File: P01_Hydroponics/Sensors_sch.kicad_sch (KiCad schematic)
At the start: 9 parts, among them J2 JST_PH_3P_TEMP, J3 JST_PH_3P_FLOW, J4 JST_PH_3P_WLS1, J5 JST_PH_4P_WLS0, J6 JST_PH_2P_PUMP, Q2 NMOS

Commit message: Need review
Please review the schematics.
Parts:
- removed J4: JST_PH_3P_WLS1, symbol Connector:Conn_01x03_Socket
- removed J5: JST_PH_4P_WLS0, symbol Connector:Conn_01x04_Socket
- added J4: JST_PH_3P_TEMP, symbol Connector:Conn_01x03_Pin
- added J5: JST_PH_3P_WLS1, symbol Connector:Conn_01x03_Socket
- added J8: JST_PH_3P_LED_EXT, symbol Connector:Conn_01x03_Socket
- added Q6: NMOS, symbol Simulation_SPICE:NMOS
- added Q7: BSS138, Package_TO_SOT_SMD:SOT-23, symbol Transistor_FET:BSS138
- added R38: 4.7k, symbol Device:R_Small
- added R39: 2k, symbol Device:R_Small
- added R40, R41, R42: 10k, symbol Device:R_Small
- J3: value JST_PH_3P_FLOW -> JST_PH_3P_WLS0
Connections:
- net GND: now also J2.3 (Pin_3), J3.3 (Pin_3), R17.2, J5.3 (Pin_3), J8.3 (Pin_3), Q6.3 (S), R40.2
- net at R17.1: now also Q2.2 (G), R16.2
- net +3.3V: now reaches J2.1 (Pin_1)
- net +3.3V: now also J3.2 (Pin_2), J5.2 (Pin_2), J8.1 (Pin_1), Q7.1 (G), R38.1, R41.1
- net TEMP_DATA: now reaches J2.2 (Pin_2)
- net TEMP_DATA: now also R38.2
- net +12V: now reaches D5.1 (K), J6.1 (Pin_1)
- net +12V: now also J4.1 (Pin_1), R42.1
- net WLS0: now reaches J3.1 (Pin_1)
- net PUMP_PWM: now reaches R16.1
- new net: Q6.2 (G), R39.2, R40.1
- new net: J4.3 (Pin_3), Q6.1 (D)
- new net DOUT: J8.2 (Pin_2)
- new net FLOW: J4.2 (Pin_2), Q7.3 (D), R42.2
- new net FLOW_DATA: Q7.2 (S), R41.2
- new net FLOW_EN: R39.1
- new net WLS1: J5.1 (Pin_1)
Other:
- note added: "Adressable LED Expansion I/O"
- note added: "DS18B20 Temperature Sensor"
- note added: "Non-contact water level switches"
- note added: "Water flow sensor"
- note added: "Water flow voltage level shifter"
- moved on the sheet: D5, J2, J6, Q2, R16, R17

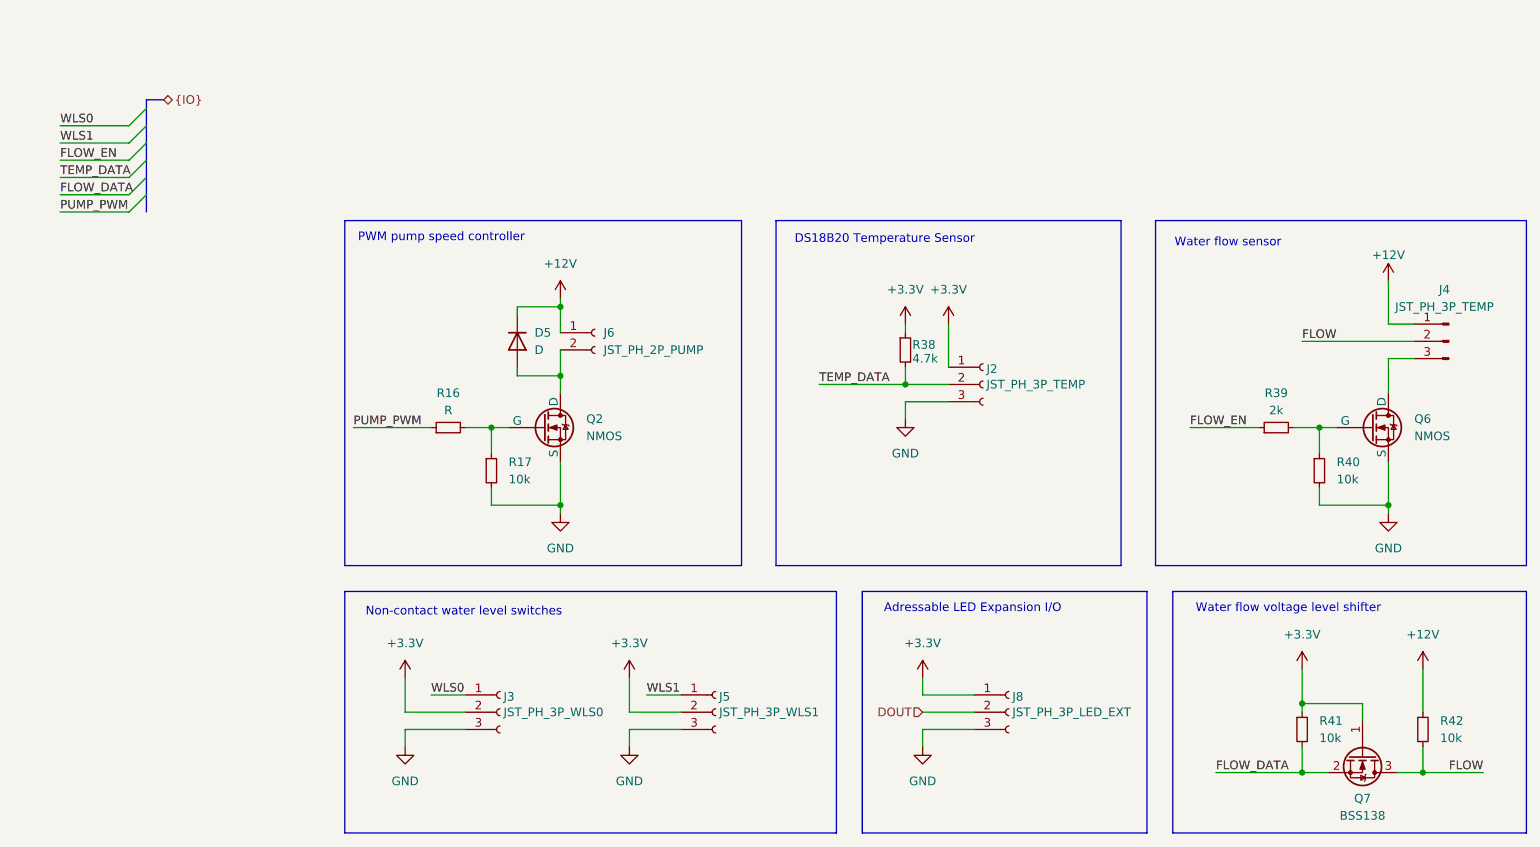
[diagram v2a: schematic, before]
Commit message: Need review
Updated:
STD14 to tag connect.
Added most footprints.
Change crystal to oscillator for ESP32
Rearrange radio controller schematic.
Added NOR flash.
Added USB-C connector for ESP32
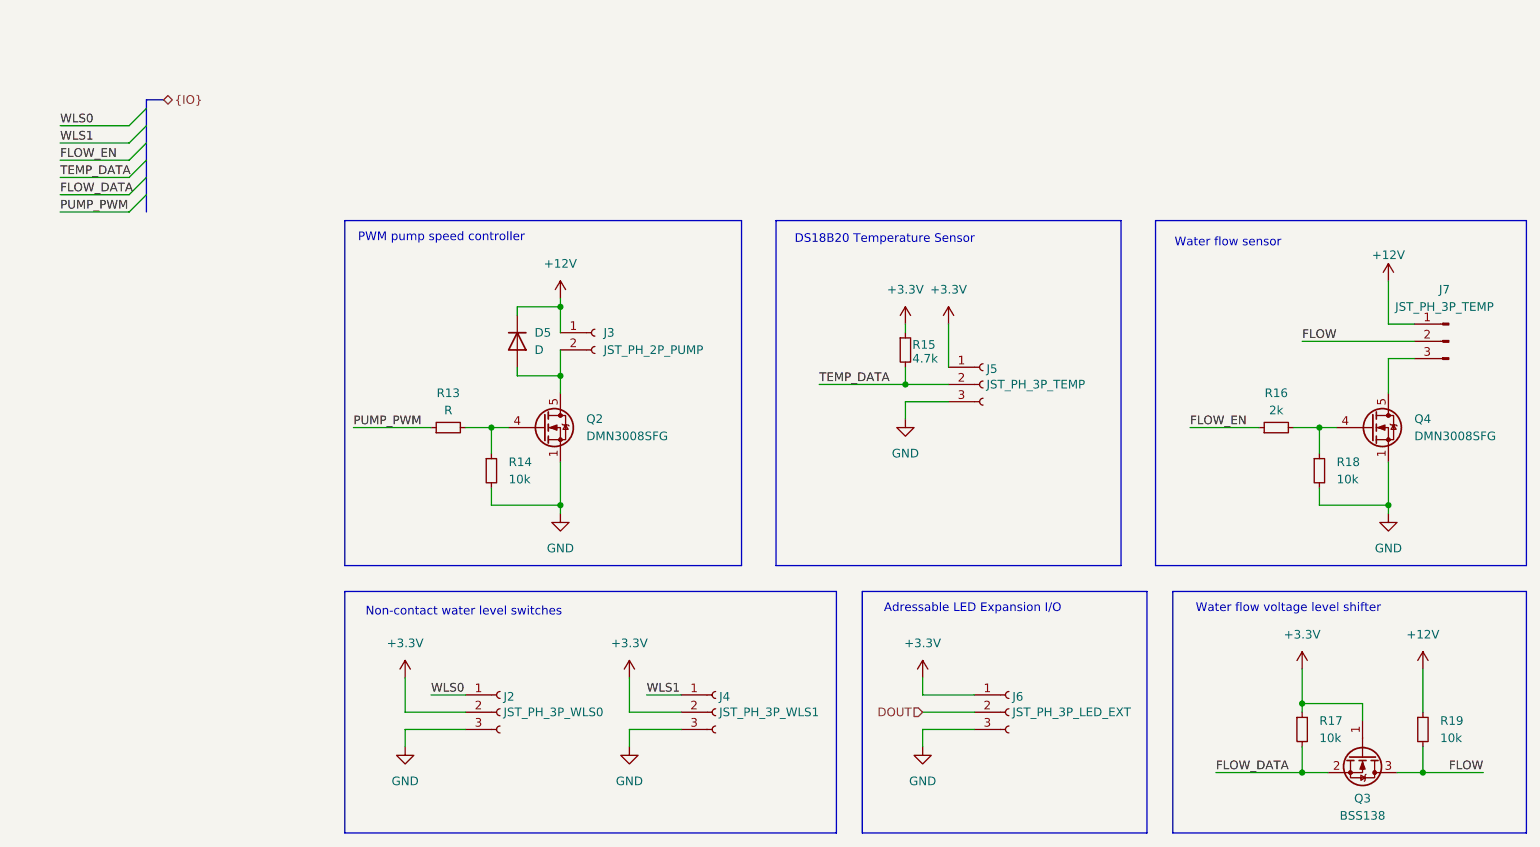
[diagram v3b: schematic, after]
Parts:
- removed Q2, Q6: NMOS, symbol Simulation_SPICE:NMOS
- added Q2, Q4: DMN3008SFG, Package_SON:Diodes_PowerDI3333-8, symbol Transistor_FET:DMN3008SFG
- R13: renamed from R16; footprint (none) -> Resistor_SMD:R_0603_1608Metric_Pad0.98x0.95mm_HandSolder
- R14: renamed from R17; footprint (none) -> Resistor_SMD:R_0603_1608Metric_Pad0.98x0.95mm_HandSolder
- R15: renamed from R38; footprint (none) -> Resistor_SMD:R_0603_1608Metric_Pad0.98x0.95mm_HandSolder
- R16: renamed from R39; footprint (none) -> Resistor_SMD:R_0603_1608Metric_Pad0.98x0.95mm_HandSolder
- R17: renamed from R41; footprint (none) -> Resistor_SMD:R_0603_1608Metric_Pad0.98x0.95mm_HandSolder
- R18: renamed from R40; footprint (none) -> Resistor_SMD:R_0603_1608Metric_Pad0.98x0.95mm_HandSolder
- R19: renamed from R42; footprint (none) -> Resistor_SMD:R_0603_1608Metric_Pad0.98x0.95mm_HandSolder
- renumbered J3 to J2, J6 to J3, J5 to J4, J2 to J5, J8 to J6, J4 to J7, Q7 to Q3
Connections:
- net GND: now also Q2.1 (S), Q2.2 (S), Q2.3 (S), Q4.1 (S), Q4.2 (S), Q4.3 (S)
- net at R16.2, R18.1: now also Q4.4 (G)
- net at R13.2, R14.1: now also Q2.4 (G)
- net at J7.3 (Pin_3): now also Q4.5 (D)
- net at D5.2 (A), J3.2 (Pin_2): now also Q2.5 (D)
